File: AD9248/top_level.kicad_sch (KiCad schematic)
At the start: 6 parts, among them J1 Conn_Coaxial, J2 Conn_Coaxial, J3 Conn_Coaxial, J4 Conn_Coaxial, U4 PPPC062LJBN-RC, U6 PPPC062LJBN-RC

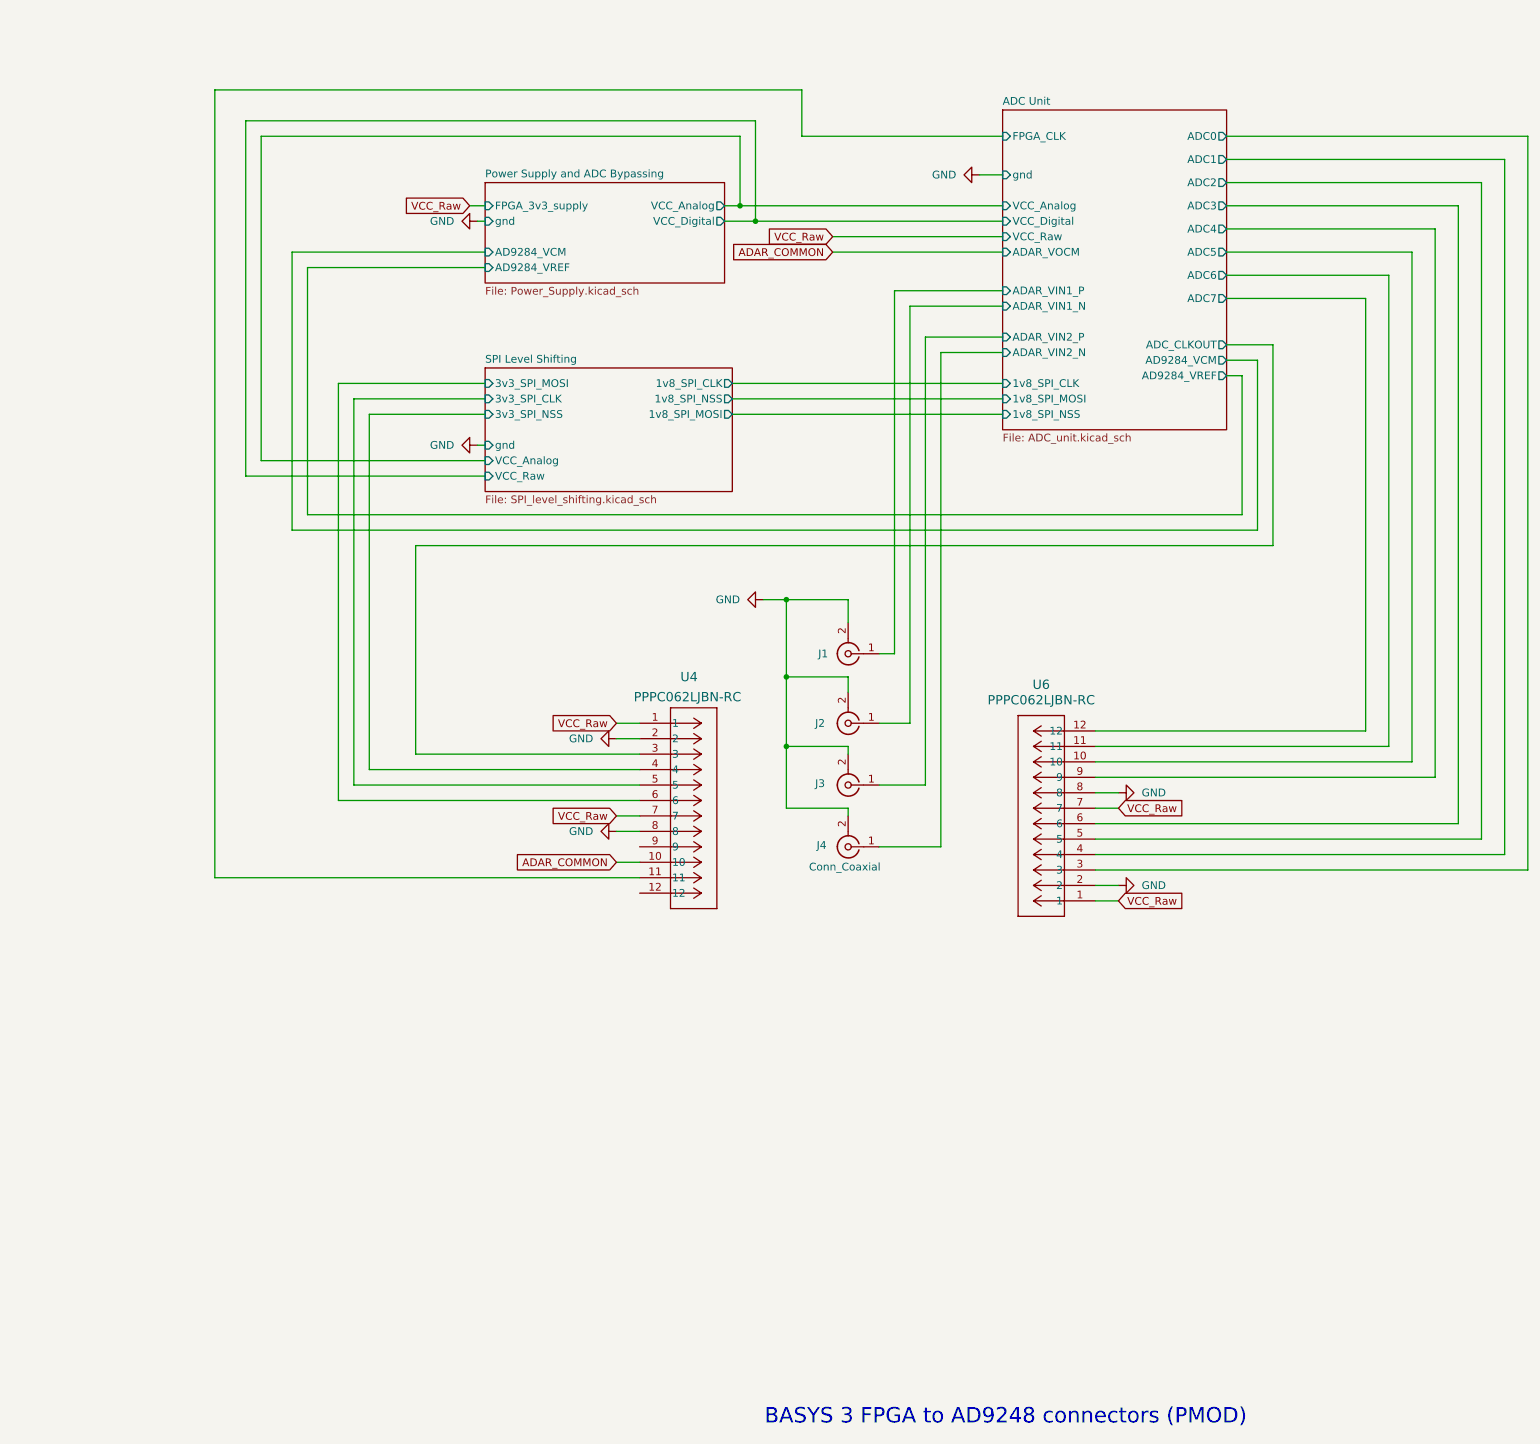
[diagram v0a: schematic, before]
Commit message: Finished and reviewed schematic, one change so far needs to be made: OE pin on level shifters must be externally toggled instead of tied to VCC. The IC requires VDDA/B to be fully ramped before pulling the OE high.
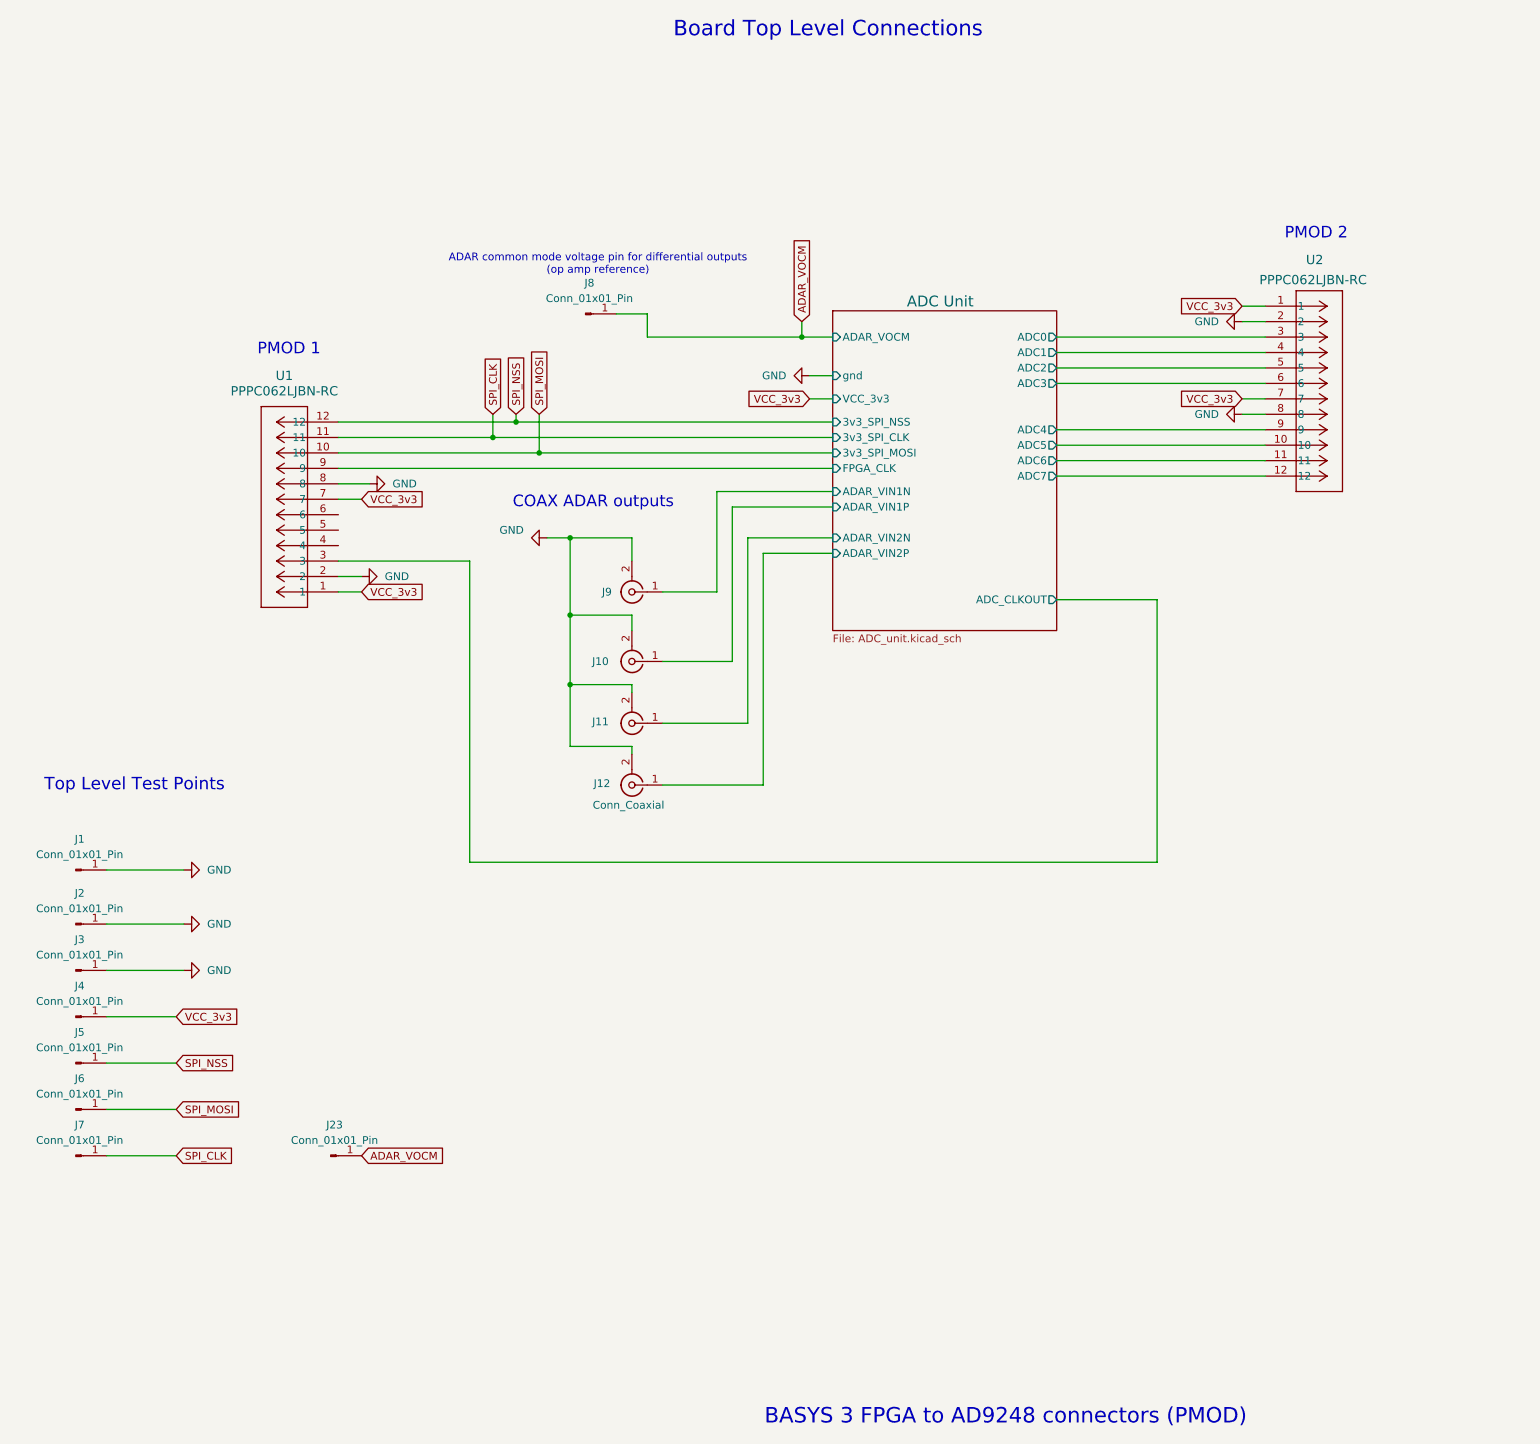
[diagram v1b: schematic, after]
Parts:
- added J1, J2, J23, J3, J4, J5, J6, J7, J8: Conn_01x01_Pin, symbol Connector:Conn_01x01_Pin
- renumbered J2 to J10, J3 to J11, J4 to J12, J1 to J9, U6 to U1, U4 to U2
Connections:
- net ADAR_COMMON is gone; now on net ADC Unit/ADC5: U2.10
- net SPI Level Shifting/3v3_SPI_CLK is gone; now on net ADC Unit/ADC2: U2.5
- net SPI Level Shifting/3v3_SPI_MOSI is gone; now on net ADC Unit/ADC3: U2.6
- net SPI Level Shifting/3v3_SPI_NSS is gone; now on net ADC Unit/ADC1: U2.4
- net ADC Unit/ADC0: now also U2.3; no longer U1.3
- net ADC Unit/ADC1: no longer U1.4
- net ADC Unit/ADC2: no longer U1.5
- net ADC Unit/ADC3: no longer U1.6
- net ADC Unit/ADC4: now also U2.9; no longer U1.9
- net ADC Unit/ADC5: no longer U1.10
- net ADC Unit/ADC6: now also U2.11; no longer U1.11
- net ADC Unit/ADC7: now also U2.12; no longer U1.12
- net ADC Unit/ADC_CLKOUT: now also U1.3; no longer U2.3
- net ADC Unit/FPGA_CLK: now also U1.9; no longer U2.11
- net GND: now also J1.1 (Pin_1), J2.1 (Pin_1), J3.1 (Pin_1)
- net ADC Unit/ADAR_VIN1_N renamed ADC Unit/ADAR_VIN1P
- net ADC Unit/ADAR_VIN1_P renamed ADC Unit/ADAR_VIN1N
- net ADC Unit/ADAR_VIN2_N renamed ADC Unit/ADAR_VIN2P
- net ADC Unit/ADAR_VIN2_P renamed ADC Unit/ADAR_VIN2N
- net VCC_Raw renamed VCC_3v3
- net VCC_3v3: now also J4.1 (Pin_1)
- new net ADAR_VOCM: J23.1 (Pin_1), J8.1 (Pin_1)
- new net SPI_CLK: J7.1 (Pin_1), U1.11
- new net SPI_MOSI: J6.1 (Pin_1), U1.10
- new net SPI_NSS: J5.1 (Pin_1), U1.12
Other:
- removed sheet Power Supply and ADC Bypassing
- removed sheet SPI Level Shifting
- sheet ADC Unit ports: added 3v3_SPI_CLK, 3v3_SPI_MOSI, 3v3_SPI_NSS, ADAR_VIN1N, ADAR_VIN1P, ADAR_VIN2N, ADAR_VIN2P, VCC_3v3; removed 1v8_SPI_CLK, 1v8_SPI_MOSI, 1v8_SPI_NSS, AD9284_VCM, AD9284_VREF, ADAR_VIN1_N, ADAR_VIN1_P, ADAR_VIN2_N, ADAR_VIN2_P, VCC_Analog, VCC_Digital, VCC_Raw
- note added: "ADAR common mode voltage pin for differential outputs (op amp reference)"
- note added: "Board Top Level Connections"
- note added: "COAX ADAR outputs"
- note added: "PMOD 1"
- note added: "PMOD 2"
- note added: "Top Level Test Points"
- title: Top Level ADC -> Top Level Connections
- moved on the sheet: J10, J11, J12, J9, U1, U2
